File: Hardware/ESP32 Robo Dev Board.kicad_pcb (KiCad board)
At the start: 2 copper layers, 61.3 x 61.3 mm, 67 parts, among them J1 PRG, U1 ESP32-S3-WROOM-1, U2 AMS1117-3.3, U3 STSPIN250, U4 STSPIN250, U5 TCA9548ARGER

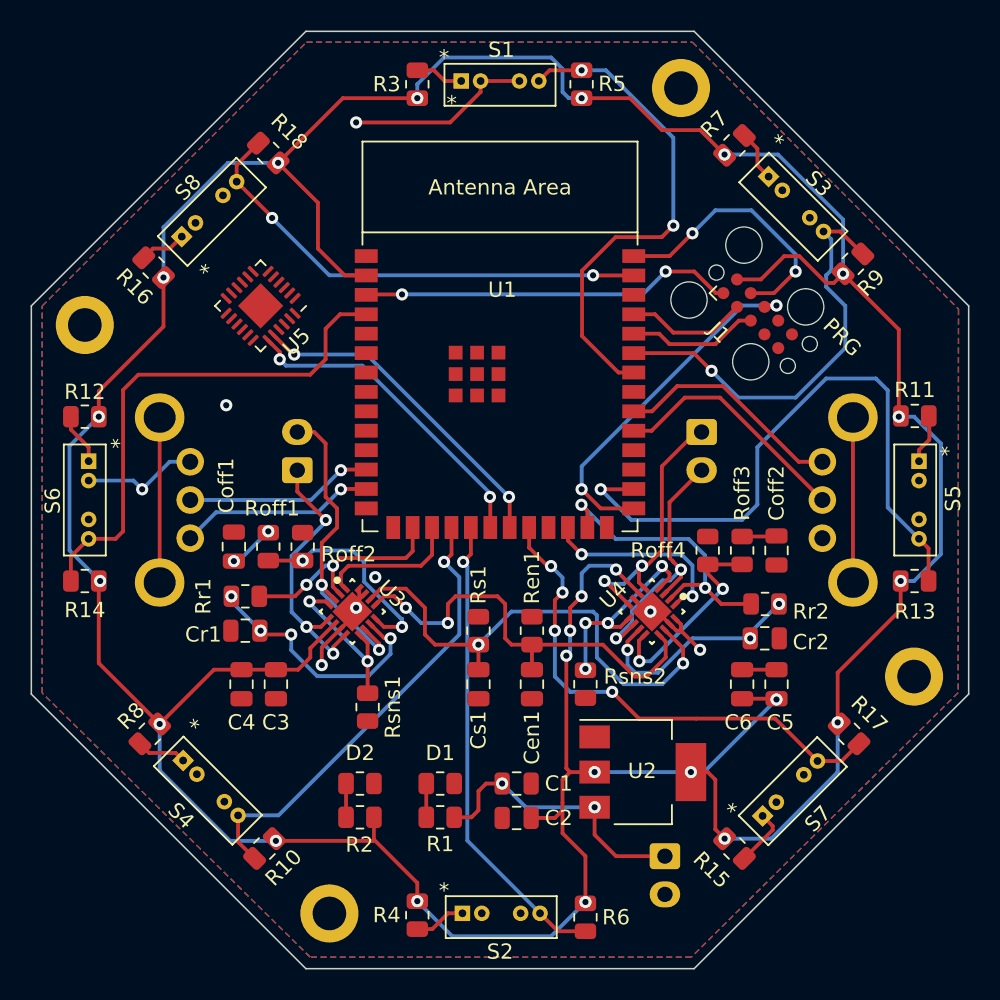
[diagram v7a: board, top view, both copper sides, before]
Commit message: Add new array for sensors
Add in sensor array

Begin trace reroute
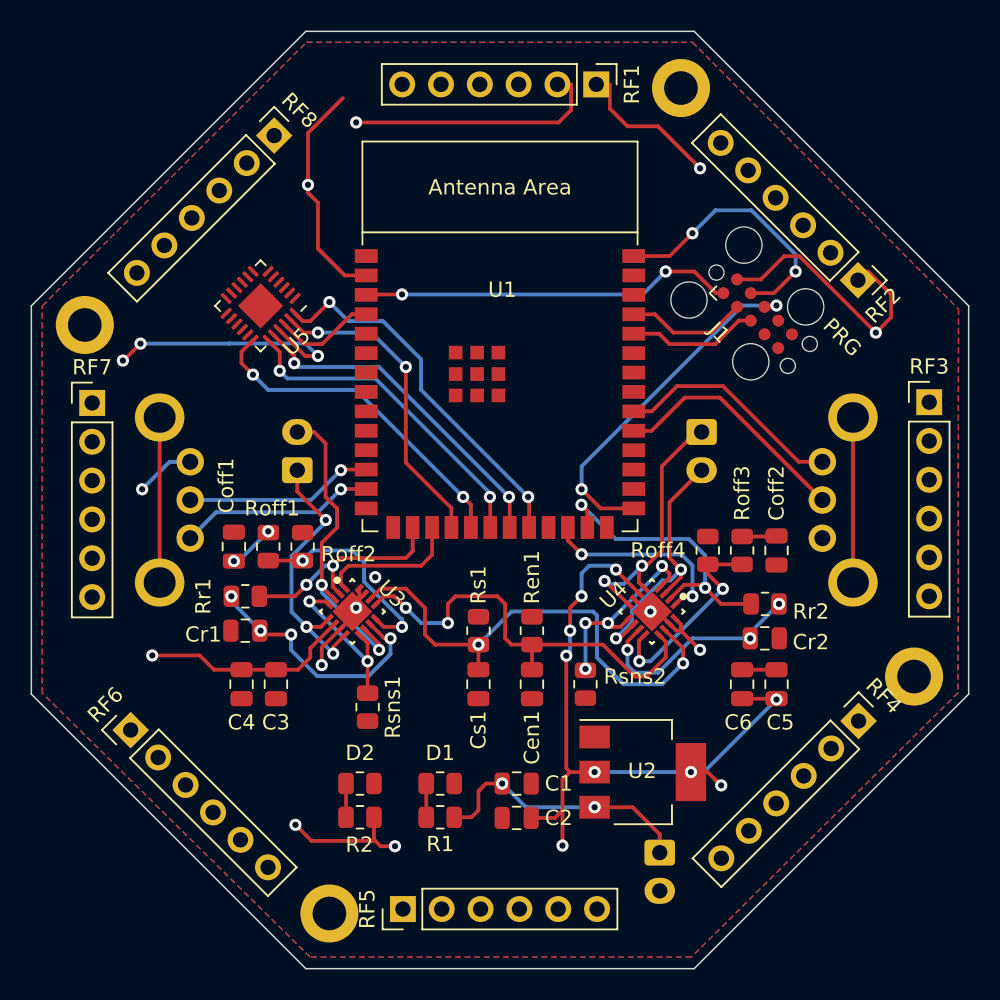
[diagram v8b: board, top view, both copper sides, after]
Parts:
- removed R10, R13, R14, R17, R18, R5, R6, R9: 1.5K, Resistor_SMD:R_0805_2012Metric
- removed R11, R12, R15, R16, R3, R4, R7, R8: 550R, Resistor_SMD:R_0805_2012Metric
- removed S1, S2, S3, S4, S5, S6, S7, S8: TCRT5000L, Amoskeag_KiCAD_Lib:TCRT5000L
- added RF1: Conn_01x06_Female, Connector_PinHeader_2.54mm:PinHeader_1x06_P2.54mm_Vertical, F.Cu at (145.0, 60.5)
- added RF2: Conn_01x06_Female, Connector_PinHeader_2.54mm:PinHeader_1x06_P2.54mm_Vertical, F.Cu at (162.1, 73.3)
- added RF3: Conn_01x06_Female, Connector_PinHeader_2.54mm:PinHeader_1x06_P2.54mm_Vertical, F.Cu at (166.7, 81.3)
- added RF4: Conn_01x06_Female, Connector_PinHeader_2.54mm:PinHeader_1x06_P2.54mm_Vertical, F.Cu at (162.1, 102.2)
- added RF5: Conn_01x06_Female, Connector_PinHeader_2.54mm:PinHeader_1x06_P2.54mm_Vertical, F.Cu at (132.3, 114.5)
- added RF6: Conn_01x06_Female, Connector_PinHeader_2.54mm:PinHeader_1x06_P2.54mm_Vertical, F.Cu at (114.5, 102.8)
- added RF7: Conn_01x06_Female, Connector_PinHeader_2.54mm:PinHeader_1x06_P2.54mm_Vertical, F.Cu at (112.0, 81.3)
- added RF8: Conn_01x06_Female, Connector_PinHeader_2.54mm:PinHeader_1x06_P2.54mm_Vertical, F.Cu at (123.9, 63.9)
- moved J_B2 0.41 mm to (149.1, 110.8)
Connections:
- U1 pad 18: /IR6 -> /A1
- U1 pad 19: /IR5 -> /A2
- U1 pad 22: /IR4 -> /I2C_Reset
- U1 pad 34: /IR1 -> unconnected-(U1-Pad34)
- U1 pad 35: /IR2 -> unconnected-(U1-Pad35)
- U1 pad 39: /IR8 -> unconnected-(U1-Pad39)
- U1 pad 4: /IR7 -> /A0
- U5 pad 1: unconnected-(U5-Pad1) -> /RF1_D
- U5 pad 10: unconnected-(U5-Pad10) -> /RF5_D
- U5 pad 11: unconnected-(U5-Pad11) -> /RF5_C
- U5 pad 12: unconnected-(U5-Pad12) -> /RF6_D
- U5 pad 13: unconnected-(U5-Pad13) -> /RF6_C
- U5 pad 14: unconnected-(U5-Pad14) -> /RF7_D
- U5 pad 15: unconnected-(U5-Pad15) -> /RF7_C
- U5 pad 16: unconnected-(U5-Pad16) -> /RF8_D
- U5 pad 17: unconnected-(U5-Pad17) -> /RF8_C
- U5 pad 18: unconnected-(U5-Pad18) -> /A2
- U5 pad 2: unconnected-(U5-Pad2) -> /RF1_C
- U5 pad 21: unconnected-(U5-Pad21) -> +3V3
- U5 pad 22: unconnected-(U5-Pad22) -> /A0
- U5 pad 23: unconnected-(U5-Pad23) -> /A1
- U5 pad 24: unconnected-(U5-Pad24) -> /I2C_Reset
- U5 pad 3: unconnected-(U5-Pad3) -> /RF2_D
- U5 pad 4: unconnected-(U5-Pad4) -> /RF2_C
- U5 pad 5: unconnected-(U5-Pad5) -> /RF3_D
- U5 pad 6: unconnected-(U5-Pad6) -> /RF3_C
- U5 pad 7: unconnected-(U5-Pad7) -> /RF4_D
- U5 pad 8: unconnected-(U5-Pad8) -> /RF4_C
- U5 pad 9: unconnected-(U5-Pad9) -> GND
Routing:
- net +3V3: track 270.7 -> 125.9 mm, vias 23 -> 18
- net /IR3: track 41.7 -> 0.03 mm, vias 1 -> 0
- net /IR7: track 34.1 -> 0.00 mm
- net /IR4: track 33.6 -> 0.00 mm, vias 4 -> 0
- net /IR1: track 32.5 -> 0.00 mm, vias 2 -> 0
- net /IR8: track 31.7 -> 0.00 mm, vias 2 -> 0
- net /IR5: track 31.0 -> 0.00 mm, vias 1 -> 0
- net /IR6: track 30.3 -> 0.00 mm, vias 1 -> 0
- net /IR2: track 28.1 -> 0.00 mm, vias 1 -> 0
- net /I2C_Reset: track 0.00 -> 24.5 mm, vias 0 -> 2
- net /A2: track 0.00 -> 22.2 mm, vias 0 -> 2
- net /A1: track 0.00 -> 20.6 mm, vias 0 -> 2
- net /A0: track 0.00 -> 6.71 mm
- net Net-(R15-Pad2): track 3.82 -> 0.00 mm
- net Net-(R12-Pad2): track 3.39 -> 0.00 mm
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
